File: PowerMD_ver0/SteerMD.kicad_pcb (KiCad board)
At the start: 2 copper layers, 75 x 88 mm, 216 parts, among them P1 SWD, P10 OUT_1, P11 ENC_0, P13 ENC_1, P14 I/O_1, P15 OUT_0, P2 MOTOR_COOLING, P3 CAN, P4 CAN, P5 SERIAL, P6 I/O_0, P7 FAN, P8 BATT_IN, P9 BATT_IN, Q1 MOSFET_N, Q2 MOSFET_N, Q3 MOSFET_N, Q4 MOSFET_N, Q5 MOSFET_N, Q6 MOSFET_N, Q7 MOSFET_N, Q8 MOSFET_N, SW1 RST, SW3 SW0, SW4 SW1, U1 MAX3051, U10 ACS758, U11 POWER_ON, U12 SI8274, U13 ACS758, U14 SI8274, U15 AZ1086H, U16 LOGO, U17 AQM0802, U19 ADRESS, U2 BD9G101, U3 STM32F405RG, U4 SI8274, U5 SI8900, U6 ADC_~RST, U7 BD9G101G, U8 SI8274, U9 BD33FA1, Y1 8MHz

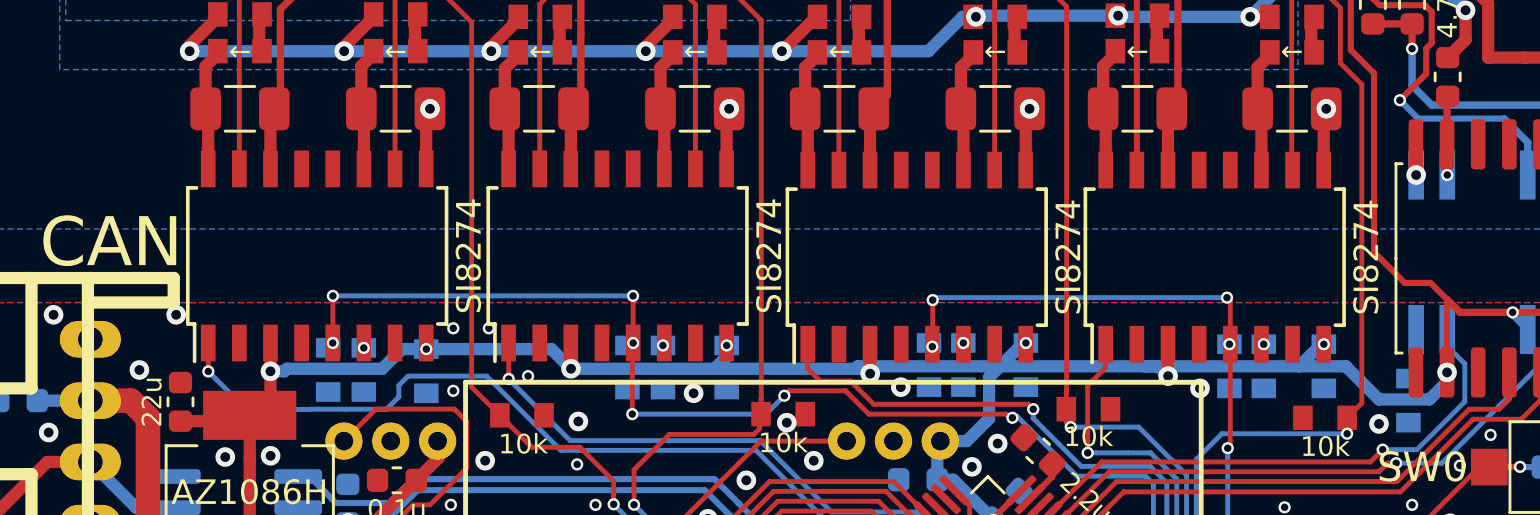
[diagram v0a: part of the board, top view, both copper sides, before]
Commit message: Power MD 電流センシングをローサイドでセンシングするように変更した&DAC乗っけた
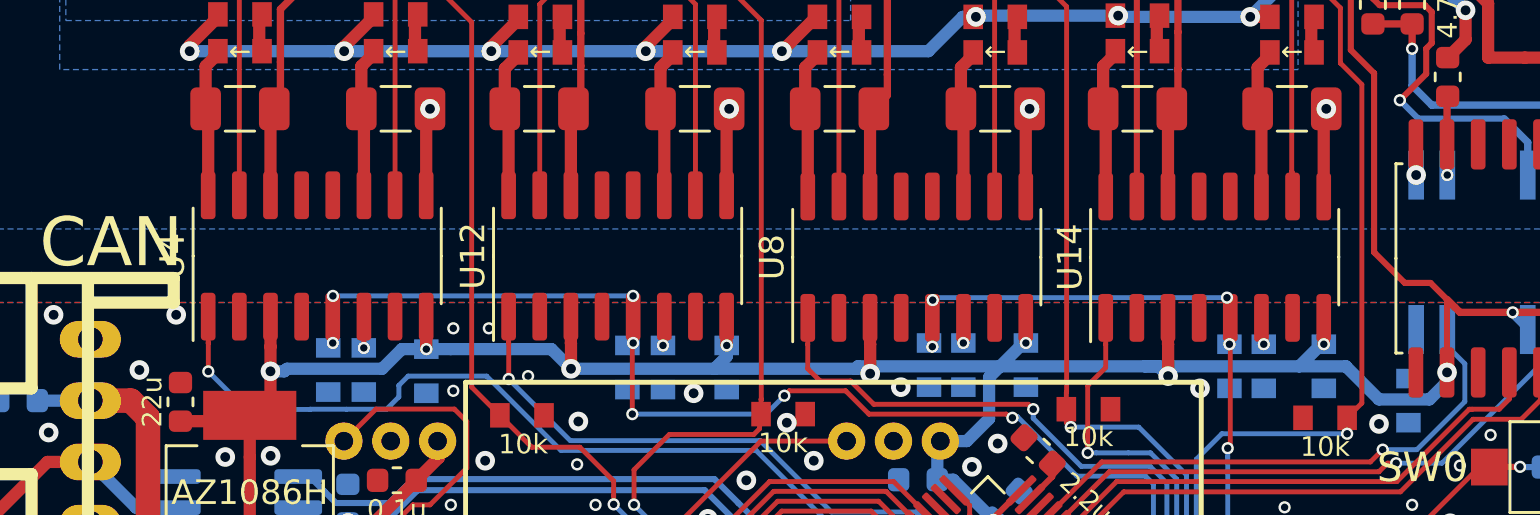
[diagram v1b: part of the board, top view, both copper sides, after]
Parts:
- U12, U14, U4, U8: footprint Package_SO:SOIC-16W_5.3x10.2mm_P1.27mm -> Package_SO:SOIC-16_3.9x9.9mm_P1.27mm
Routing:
- net +3V3: track 289.3 -> 298.4 mm
- net Net-(R11-Pad1): track 0.00 -> 1.28 mm
- net Net-(R35-Pad1): track 0.00 -> 1.20 mm
- net Net-(R65-Pad1): track 0.00 -> 1.11 mm
- net /PWM1_R: track 16.3 -> 17.4 mm
- net /PWM1_L: track 23.2 -> 24.3 mm
- net /PWM0_R: track 29.8 -> 30.9 mm
- net /PWM0_L: track 43.9 -> 44.9 mm
- net Net-(R13-Pad1): track 0.00 -> 1.03 mm

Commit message: ねむねむ。( ˘ω˘)ｽﾔｧ
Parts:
- R19, R20, R28, R29, R55, R56, R58, R59: value 1 -> 10
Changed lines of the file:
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@@
       (effects (font (size 1.2065 1.2065) (thickness 0.1016)) (justify left bottom))
     )
-    (fp_text value 1 (at 0 -0.7) (layer F.SilkS)
+    (fp_text value 10 (at 0 -0.7) (layer F.SilkS)
       (effects (font (size 0.8 0.8) (thickness 0.15)) (justify bottom))
     )
@@
       (effects (font (size 1.2065 1.2065) (thickness 0.1016)) (justify left bottom))
     )
-    (fp_text value 1 (at 0 -0.7) (layer F.SilkS)
+    (fp_text value 10 (at 0 -0.7) (layer F.SilkS)
       (effects (font (size 0.8 0.8) (thickness 0.15)) (justify bottom))
     )
@@
       (effects (font (size 1.2065 1.2065) (thickness 0.1016)) (justify left bottom))
     )
-    (fp_text value 1 (at 0 -0.65) (layer F.SilkS)
+    (fp_text value 10 (at 0 -0.65) (layer F.SilkS)
       (effects (font (size 0.8 0.8) (thickness 0.2)) (justify bottom))
     )
@@
       (effects (font (size 1.2065 1.2065) (thickness 0.1016)) (justify left bottom))
     )
-    (fp_text value 1 (at 0 -0.65) (layer F.SilkS)
+    (fp_text value 10 (at 0 -0.65) (layer F.SilkS)
       (effects (font (size 0.8 0.8) (thickness 0.2)) (justify bottom))
     )
@@
       (effects (font (size 1.2065 1.2065) (thickness 0.1016)) (justify left bottom))
     )
-    (fp_text value 1 (at 0 -0.65) (layer F.SilkS)
+    (fp_text value 10 (at 0 -0.65) (layer F.SilkS)
       (effects (font (size 0.8 0.8) (thickness 0.2)) (justify bottom))
     )
@@
       (effects (font (size 1.2065 1.2065) (thickness 0.1016)) (justify left bottom))
     )
-    (fp_text value 1 (at 0 -0.65) (layer F.SilkS)
+    (fp_text value 10 (at 0 -0.65) (layer F.SilkS)
       (effects (font (size 0.8 0.8) (thickness 0.2)) (justify bottom))
     )
@@
       (effects (font (size 1.2065 1.2065) (thickness 0.1016)) (justify left bottom))
     )
-    (fp_text value 1 (at 0 -0.65) (layer F.SilkS)
+    (fp_text value 10 (at 0 -0.65) (layer F.SilkS)
       (effects (font (size 0.8 0.8) (thickness 0.2)) (justify bottom))
     )
@@
       (effects (font (size 1.2065 1.2065) (thickness 0.1016)) (justify left bottom))
     )
-    (fp_text value 1 (at 0 -0.65) (layer F.SilkS)
+    (fp_text value 10 (at 0 -0.65) (layer F.SilkS)
       (effects (font (size 0.8 0.8) (thickness 0.2)) (justify bottom))
     )

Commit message: 電流制御MDをだいぶ進めた
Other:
- board text added: "Vdd"
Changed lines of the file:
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@@
     (effects (font (size 0.8 0.8) (thickness 0.15)))
   )
-  (gr_text 5V (at 121.95 127.2 90) (layer B.SilkS)
+  (gr_text Vdd (at 121.95 127.2 90) (layer B.SilkS)
     (effects (font (size 0.8 0.8) (thickness 0.15)) (justify mirror))
   )
@@
     (effects (font (size 0.8 0.8) (thickness 0.15)) (justify mirror))
   )
-  (gr_text 5V (at 132 128) (layer B.SilkS)
+  (gr_text Vdd (at 132 128) (layer B.SilkS)
     (effects (font (size 0.8 0.8) (thickness 0.15)) (justify mirror))
   )

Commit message: 電流制御MD(仮)配線(仮)完成(仮)
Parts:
- R37: value 50k -> 3.9k
- R38: value 10k -> 680
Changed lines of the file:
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@@
       (effects (font (size 1 1) (thickness 0.15)) (justify mirror))
     )
-    (fp_text value 50k (at -2.45 0 90) (layer B.SilkS)
+    (fp_text value 3.9k (at -2.45 0 90) (layer B.SilkS)
       (effects (font (size 0.8 0.8) (thickness 0.15)) (justify mirror))
     )
@@
       (effects (font (size 1 1) (thickness 0.15)) (justify mirror))
     )
-    (fp_text value 10k (at 2.5 0) (layer B.SilkS)
+    (fp_text value 680 (at 2.5 0) (layer B.SilkS)
       (effects (font (size 0.8 0.8) (thickness 0.15)) (justify mirror))
     )

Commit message: いろいろ修正しました
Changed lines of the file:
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@@
       (effects (font (size 1 1) (thickness 0.15)))
     )
-    (fp_text value SI8274 (at 0 5.9 90) (layer F.Fab)
+    (fp_text value SI8274 (at 0 5.9 90) (layer F.SilkS)
       (effects (font (size 1 1) (thickness 0.15)))
     )
@@
     (tags "SOIC SO")
     (attr smd)
-    (fp_text reference U8 (at 0 -5.9 90) (layer F.SilkS)
+    (fp_text reference U8 (at 0 -5.9 90) (layer F.SilkS) hide
       (effects (font (size 1 1) (thickness 0.15)))
     )
-    (fp_text value SI8274 (at 0 5.9 90) (layer F.Fab)
+    (fp_text value SI8274 (at 0 5.9 90) (layer F.SilkS)
       (effects (font (size 1 1) (thickness 0.15)))
     )
@@
     (tags "SOIC SO")
     (attr smd)
-    (fp_text reference U12 (at 0 -5.9 90) (layer F.SilkS)
+    (fp_text reference U12 (at 0 -5.9 90) (layer F.SilkS) hide
       (effects (font (size 1 1) (thickness 0.15)))
     )
-    (fp_text value SI8274 (at 0 5.9 90) (layer F.Fab)
+    (fp_text value SI8274 (at 0 5.9 90) (layer F.SilkS)
       (effects (font (size 1 1) (thickness 0.15)))
     )
@@
     (tags "SOIC SO")
     (attr smd)
-    (fp_text reference U14 (at 0 -5.9 90) (layer F.SilkS)
+    (fp_text reference U14 (at 0 -5.9 90) (layer F.SilkS) hide
       (effects (font (size 1 1) (thickness 0.15)))
     )
-    (fp_text value SI8274 (at 0 5.9 90) (layer F.Fab)
+    (fp_text value SI8274 (at 0 5.9 90) (layer F.SilkS)
       (effects (font (size 1 1) (thickness 0.15)))
     )
@@
       )
     )
+  )
+  (zone (net 0) (net_name "") (layer B.Cu) (hatch edge 0.508)
+    (connect_pads (clearance 0.2))
+    (min_thickness 0.254)
+    (keepout (tracks allowed) (vias allowed) (copperpour not_allowed))
+    (fill (arc_segments 32) (thermal_gap 0.508) (thermal_bridge_width 0.508))
+    (polygon
+      (pts
+        (xy 138.75 66.25) (xy 138.75 74.25) (xy 144.75 74.25) (xy 144.75 66.25)
+      )
+    )
